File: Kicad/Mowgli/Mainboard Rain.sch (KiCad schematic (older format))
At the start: 10 parts, among them Q16 (G15 Marking), U21 LM321 (A63A)

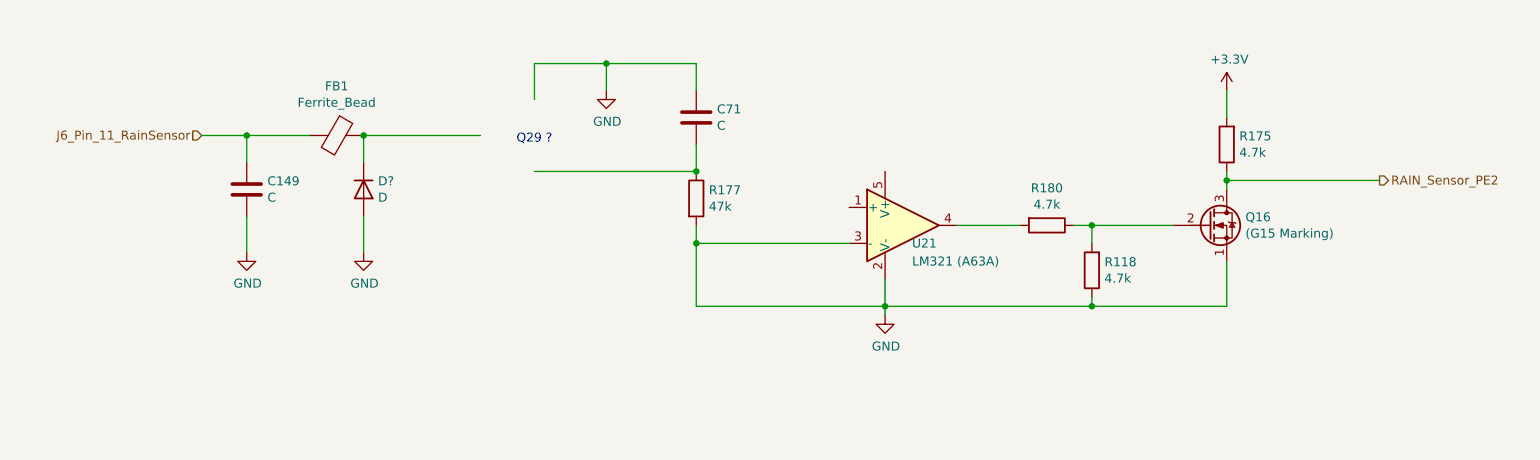
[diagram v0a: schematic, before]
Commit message: added some datasheets, kicad updates
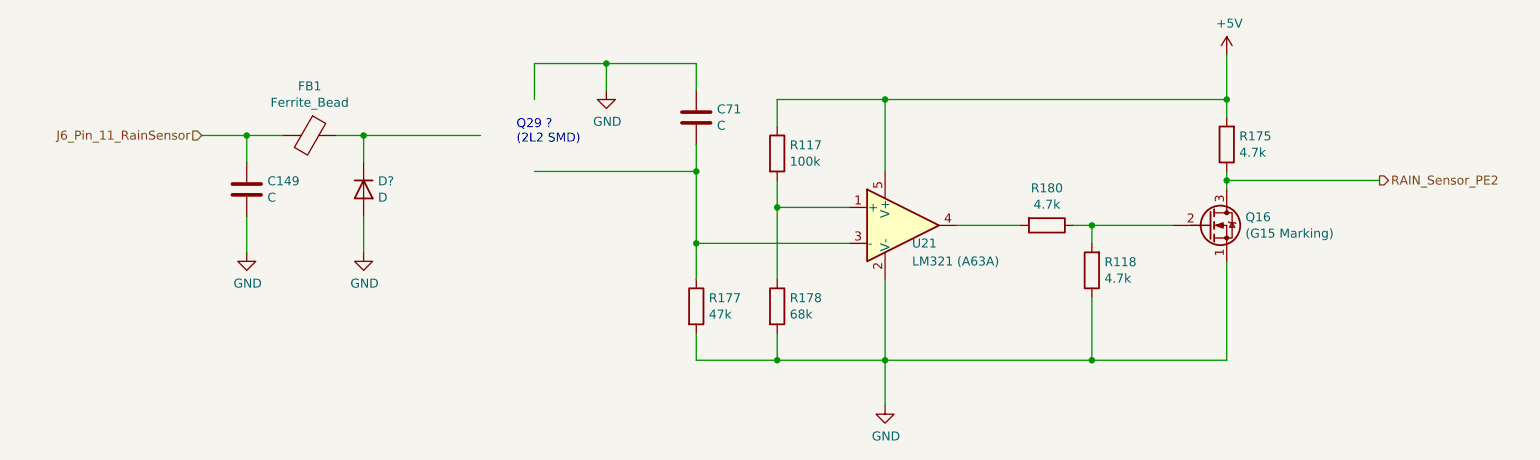
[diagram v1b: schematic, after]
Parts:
- added R117: 100k, symbol Device:R
- added R178: 68k, symbol Device:R
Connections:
- net labels added: +5V
- net labels removed: +3.3V
- wire segments 32 -> 44
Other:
- note added: "Q29 ?\n(2L2 SMD)"
- note removed: "Q29 ?"
- moved on the sheet: FB1, R177
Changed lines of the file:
@@
 $Descr A4 11693 8268
 encoding utf-8
-Sheet 12 12
+Sheet 12 13
 Title ""
 Date ""
@@
 L Device:Ferrite_Bead FB1
 U 1 1 62B99231
-P 3000 2350
-F 0 "FB1" V 2726 2350 50  0000 C CNN
-F 1 "Ferrite_Bead" V 2817 2350 50  0000 C CNN
-F 2 "" V 2930 2350 50  0001 C CNN
-F 3 "~" H 3000 2350 50  0001 C CNN
-	1    3000 2350
+P 2850 2350
+F 0 "FB1" V 2576 2350 50  0000 C CNN
+F 1 "Ferrite_Bead" V 2667 2350 50  0000 C CNN
+F 2 "" V 2780 2350 50  0001 C CNN
+F 3 "~" H 2850 2350 50  0001 C CNN
+	1    2850 2350
 	0    1    1    0
 $EndComp
-Wire Wire Line
-	2850 2350 2500 2350
 Connection ~ 2500 2350
 $Comp
 L Device:R R177
 U 1 1 62B9A40E
-P 5000 2700
-F 0 "R177" H 5070 2746 50  0000 L CNN
-F 1 "47k" H 5070 2655 50  0000 L CNN
-F 2 "" V 4930 2700 50  0001 C CNN
-F 3 "~" H 5000 2700 50  0001 C CNN
-	1    5000 2700
+P 5000 3300
+F 0 "R177" H 5070 3346 50  0000 L CNN
+F 1 "47k" H 5070 3255 50  0000 L CNN
+F 2 "" V 4930 3300 50  0001 C CNN
+F 3 "~" H 5000 3300 50  0001 C CNN
+	1    5000 3300
 	1    0    0    -1
 $EndComp
@@
 Wire Wire Line
 	5850 2950 5000 2950
-Wire Wire Line
-	5000 2850 5000 2950
-Connection ~ 5000 2950
 $Comp
 L power:GND #PWR?
 U 1 1 62B9BC4C
-P 6050 3350
-F 0 "#PWR?" H 6050 3100 50  0001 C CNN
-F 1 "GND" H 6055 3177 50  0000 C CNN
-F 2 "" H 6050 3350 50  0001 C CNN
-F 3 "" H 6050 3350 50  0001 C CNN
-	1    6050 3350
+P 6050 3850
+F 0 "#PWR?" H 6050 3600 50  0001 C CNN
+F 1 "GND" H 6055 3677 50  0000 C CNN
+F 2 "" H 6050 3850 50  0001 C CNN
+F 3 "" H 6050 3850 50  0001 C CNN
+	1    6050 3850
 	1    0    0    -1
 $EndComp
@@
 Wire Wire Line
 	7200 2850 7200 2950
-Wire Wire Line
-	7200 3250 7200 3300
-Wire Wire Line
-	7200 3300 6050 3300
-Connection ~ 6050 3300
-Wire Wire Line
-	6050 3300 6050 3350
-Wire Wire Line
-	6050 3150 6050 3300
-Wire Wire Line
-	6050 3300 5000 3300
-Wire Wire Line
-	5000 2950 5000 3300
 $Comp
 L Device:Q_NMOS_SGD Q16
@@
 $EndComp
 Wire Wire Line
-	7200 3300 7950 3300
-Wire Wire Line
-	7950 3300 7950 3050
-Connection ~ 7200 3300
-Wire Wire Line
 	7650 2850 7200 2850
 Connection ~ 7200 2850
-$Comp
-L power:+3.3V #PWR?
-U 1 1 62BA2065
-P 7950 2100
-F 0 "#PWR?" H 7950 1950 50  0001 C CNN
-F 1 "+3.3V" H 7965 2273 50  0000 C CNN
-F 2 "" H 7950 2100 50  0001 C CNN
-F 3 "" H 7950 2100 50  0001 C CNN
-	1    7950 2100
-	1    0    0    -1
-$EndComp
-Wire Wire Line
-	7950 2100 7950 2250
 Wire Wire Line
 	7950 2550 7950 2600
@@
 	4500 1950 5000 1950
 Text Notes 4000 2400 0    50   ~ 0
-Q29 ?
+Q29 ?\n(2L2 SMD)
+Wire Wire Line
+	5000 2550 5000 2950
+Connection ~ 5000 2950
+Wire Wire Line
+	5000 3600 5450 3600
+Wire Wire Line
+	6050 3150 6050 3600
+Connection ~ 6050 3600
+Wire Wire Line
+	6050 3600 6050 3850
+Wire Wire Line
+	7950 3600 7200 3600
+Wire Wire Line
+	7950 3050 7950 3600
+Wire Wire Line
+	7200 3250 7200 3600
+Connection ~ 7200 3600
+Wire Wire Line
+	7200 3600 6050 3600
+Wire Wire Line
+	5000 3450 5000 3600
+Wire Wire Line
+	5000 3150 5000 2950
+$Comp
+L Device:R R178
+U 1 1 62BB95B1
+P 5450 3300
+F 0 "R178" H 5520 3346 50  0000 L CNN
+F 1 "68k" H 5520 3255 50  0000 L CNN
+F 2 "" V 5380 3300 50  0001 C CNN
+F 3 "~" H 5450 3300 50  0001 C CNN
+	1    5450 3300
+	1    0    0    -1
+$EndComp
+Wire Wire Line
+	5450 3450 5450 3600
+Connection ~ 5450 3600
+Wire Wire Line
+	5450 3600 6050 3600
+Wire Wire Line
+	5450 3150 5450 2750
+Wire Wire Line
+	5450 2750 5850 2750
+$Comp
+L Device:R R117
+U 1 1 62BBA5A3
+P 5450 2450
+F 0 "R117" H 5520 2496 50  0000 L CNN
+F 1 "100k" H 5520 2405 50  0000 L CNN
+F 2 "" V 5380 2450 50  0001 C CNN
+F 3 "~" H 5450 2450 50  0001 C CNN
+	1    5450 2450
+	1    0    0    -1
+$EndComp
+Wire Wire Line
+	5450 2600 5450 2750
+Connection ~ 5450 2750
+Wire Wire Line
+	5450 2150 5450 2300
+Connection ~ 7950 2150
+Wire Wire Line
+	7950 2150 7950 2250
+Wire Wire Line
+	7950 1900 7950 2150
+Wire Wire Line
+	6050 2550 6050 2150
+Wire Wire Line
+	5450 2150 6050 2150
+Connection ~ 6050 2150
+Wire Wire Line
+	6050 2150 7950 2150
+$Comp
+L power:+5V #PWR?
+U 1 1 62BC05A7
+P 7950 1900
+F 0 "#PWR?" H 7950 1750 50  0001 C CNN
+F 1 "+5V" H 7965 2073 50  0000 C CNN
+F 2 "" H 7950 1900 50  0001 C CNN
+F 3 "" H 7950 1900 50  0001 C CNN
+	1    7950 1900
+	1    0    0    -1
+$EndComp
+Wire Wire Line
+	2700 2350 2500 2350
+Wire Wire Line
+	3000 2350 3150 2350
 $EndSCHEMATC
